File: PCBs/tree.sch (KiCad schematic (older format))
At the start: 31 parts, among them J1 Conn_01x06_Female, SW1 SW_Push_DPDT, SW2 SW_SPST, U1 Shift_Reg, U2 Shift_Reg, U3 Shift_Reg, U4 pic18f45k20

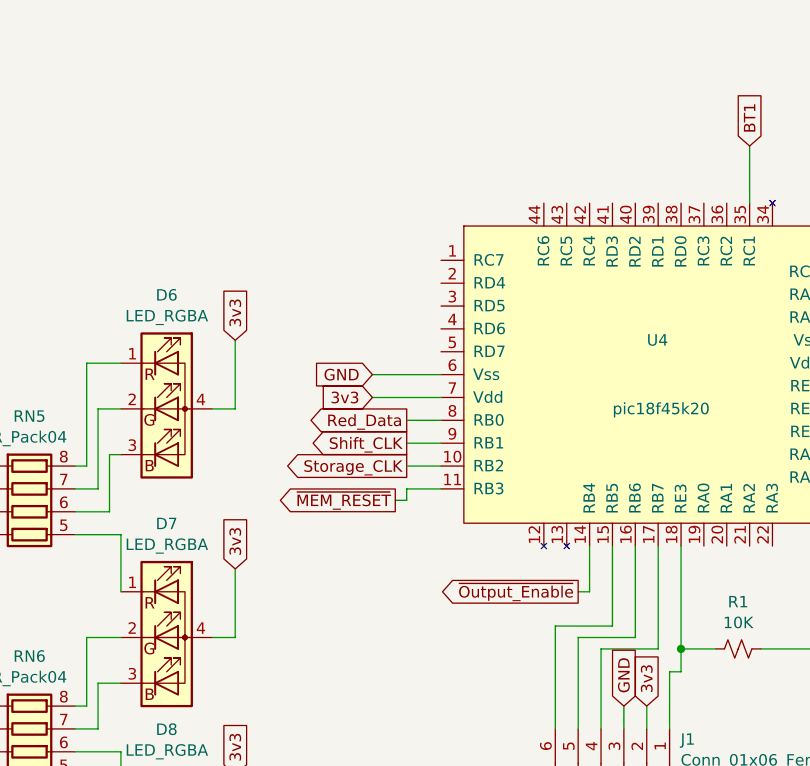
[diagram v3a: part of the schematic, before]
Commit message: Finished Bulk of routing. Reformated traces to use 6/6 mils as per board house rules.
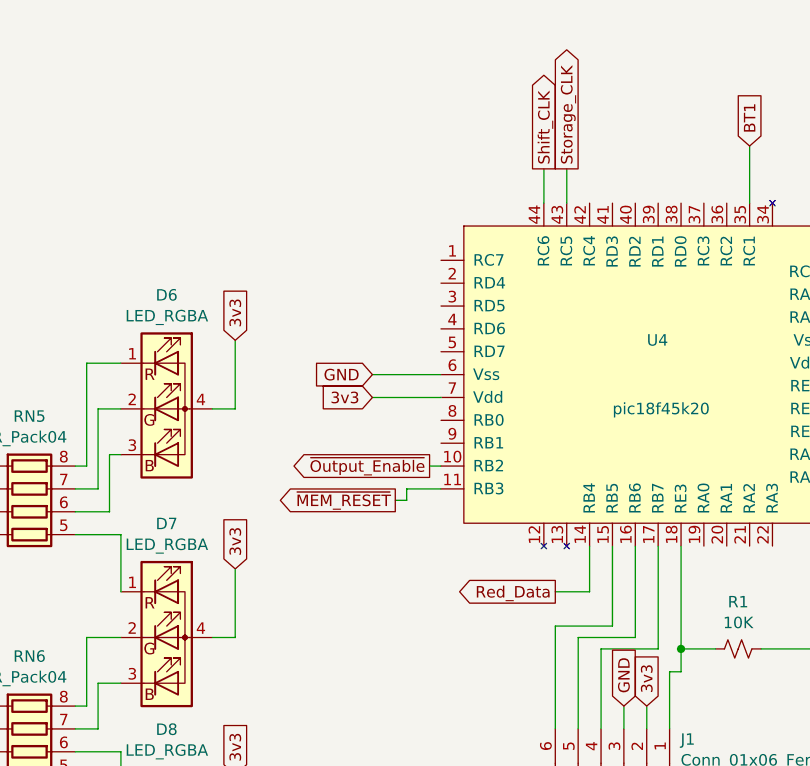
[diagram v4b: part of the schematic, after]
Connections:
- net Red_Data: now also U4.14 (RB4); no longer U4.8 (RB0)
- net Shift_CLK: now also U4.44 (RC6); no longer U4.9 (RB1)
- net Storage_CLK: now also U4.43 (RC5); no longer U4.10 (RB2)
- net ~Output_Enable~: now also U4.10 (RB2); no longer U4.14 (RB4)
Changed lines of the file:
@@
 Wire Wire Line
 	4200 3600 4050 3600
-Text GLabel 8400 2200 0    50   Output ~ 0
+Text GLabel 9050 2950 0    50   Output ~ 0
 Red_Data
 Wire Wire Line
-	8400 2200 8550 2200
+	9050 2950 9200 2950
 Text GLabel 4150 1750 2    50   Input ~ 0
 Shift_CLK
@@
 Wire Wire Line
 	4200 4250 4050 4250
-Text GLabel 8400 2300 0    50   Output ~ 0
+Text GLabel 9000 1100 1    50   Output ~ 0
 Shift_CLK
 Wire Wire Line
-	8400 2300 8550 2300
+	9000 1100 9000 1250
 Text GLabel 4150 2250 2    50   Input ~ 0
 Storage_CLK
@@
 Wire Wire Line
 	4200 4750 4050 4750
-Text GLabel 8400 2400 0    50   Output ~ 0
+Text GLabel 9100 1100 1    50   Output ~ 0
 Storage_CLK
 Wire Wire Line
-	8400 2400 8550 2400
+	9100 1100 9100 1250
 Text GLabel 2900 2300 0    50   Input ~ 0
 ~MEM_RESET~
@@
 Wire Wire Line
 	3000 4850 3150 4850
-Text GLabel 8350 2550 0    50   Output ~ 0
-~MEM_RESET~
-Text GLabel 9150 2950 0    50   Output ~ 0
+Text GLabel 8500 2400 0    50   Output ~ 0
 ~Output_Enable~
 Wire Wire Line
-	8350 2550 8400 2550
-Wire Wire Line
-	8400 2550 8400 2500
-Wire Wire Line
-	8400 2500 8550 2500
-Wire Wire Line
-	9150 2950 9200 2950
+	8500 2400 8550 2400
 Wire Wire Line
 	9200 2950 9200 2750
@@
 Wire Wire Line
 	2650 6750 2550 6750
+Wire Wire Line
+	8400 2500 8550 2500
+Wire Wire Line
+	8400 2550 8400 2500
+Wire Wire Line
+	8350 2550 8400 2550
+Text GLabel 8350 2550 0    50   Output ~ 0
+~MEM_RESET~
 $EndSCHEMATC

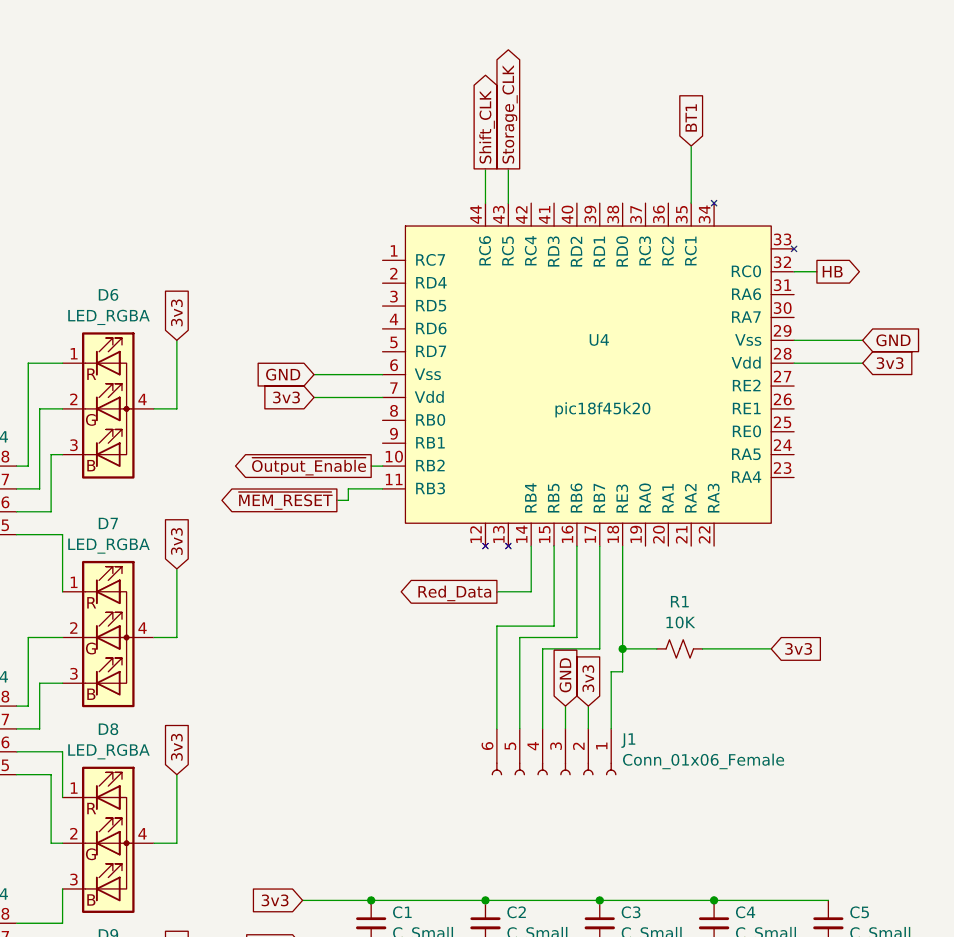
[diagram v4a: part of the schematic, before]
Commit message: Adding LPC804 as ARM processor for this branch
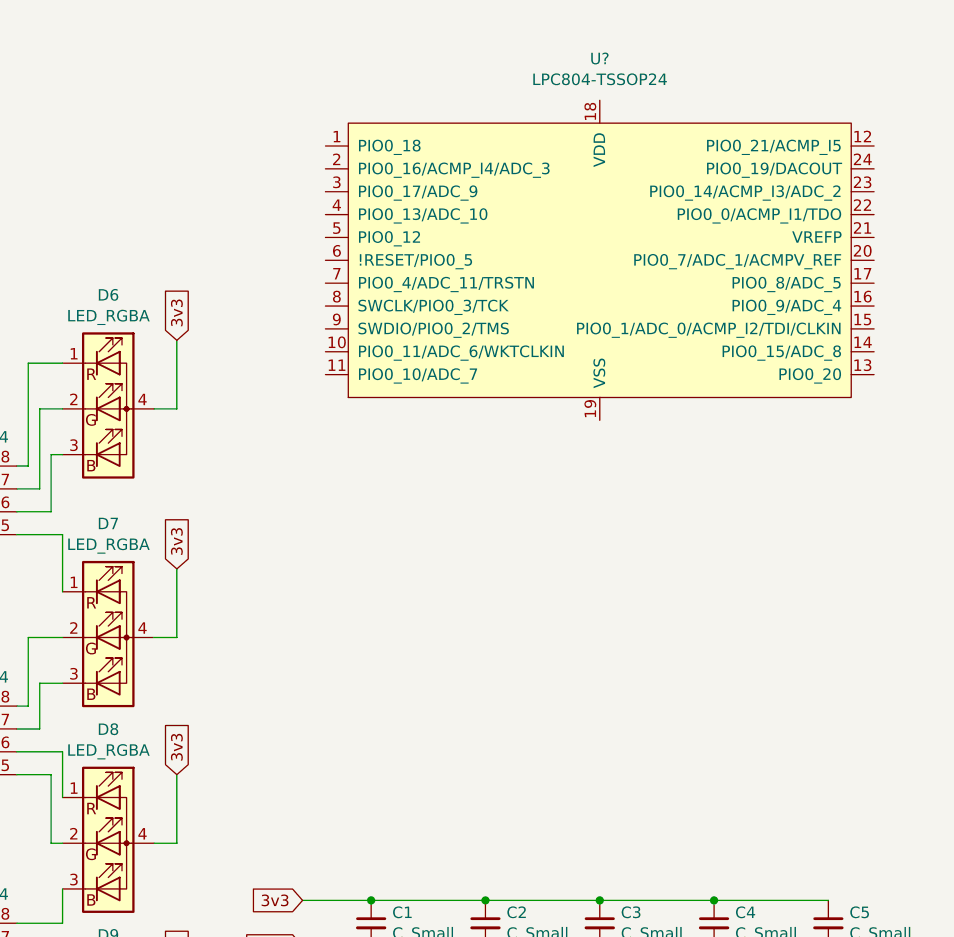
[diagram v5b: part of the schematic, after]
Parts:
- removed J1: Conn_01x06_Female, Connector_PinHeader_2.54mm:PinHeader_1x06_P2.54mm_Vertical, symbol Connector:Conn_01x06_Female
- removed R1: 10K, Resistor_SMD:R_0805_2012Metric, symbol Device:R_Small_US
- removed U4: pic18f45k20, Package_QFP:LQFP-44_10x10mm_P0.8mm, symbol pic18f45k20:pic18f45k20
- added U?: LPC804-TSSOP24, symbol MCU_NXP_LPC804:LPC804-TSSOP24
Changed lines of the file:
@@
 $EndDescr
-$Comp
-L pic18f45k20:pic18f45k20 U4
-U 1 1 6011DF0B
-P 9500 2000
-F 0 "U4" H 9450 2150 50  0000 L CNN
-F 1 "pic18f45k20" H 9300 1850 50  0000 L CNN
-F 2 "Package_QFP:LQFP-44_10x10mm_P0.8mm" H 9500 2000 50  0001 C CNN
-F 3 "" H 9500 2000 50  0001 C CNN
-	1    9500 2000
-	1    0    0    -1
-$EndComp
-$Comp
-L Connector:Conn_01x06_Female J1
-U 1 1 6011E5C4
-P 9350 3750
-F 0 "J1" V 9196 3998 50  0000 L CNN
-F 1 "Conn_01x06_Female" V 9287 3998 50  0000 L CNN
-F 2 "Connector_PinHeader_2.54mm:PinHeader_1x06_P2.54mm_Vertical" H 9350 3750 50  0001 C CNN
-F 3 "~" H 9350 3750 50  0001 C CNN
-	1    9350 3750
-	0    1    1    0
-$EndComp
-$Comp
-L Device:R_Small_US R1
-U 1 1 6011FC54
-P 9850 3200
-F 0 "R1" V 9645 3200 50  0000 C CNN
-F 1 "10K" V 9736 3200 50  0000 C CNN
-F 2 "Resistor_SMD:R_0805_2012Metric" H 9850 3200 50  0001 C CNN
-F 3 "~" H 9850 3200 50  0001 C CNN
-	1    9850 3200
-	0    1    1    0
-$EndComp
-Wire Wire Line
-	9050 3550 9050 3100
-Wire Wire Line
-	9050 3100 9300 3100
-Wire Wire Line
-	9300 3100 9300 2750
-Wire Wire Line
-	9150 3550 9150 3150
-Wire Wire Line
-	9150 3150 9400 3150
-Wire Wire Line
-	9400 3150 9400 2750
-Wire Wire Line
-	9250 3550 9250 3200
-Wire Wire Line
-	9250 3200 9500 3200
-Wire Wire Line
-	9500 3200 9500 2750
-Wire Wire Line
-	9600 2750 9600 3200
-Wire Wire Line
-	9600 3200 9750 3200
-Connection ~ 9600 3200
-Wire Wire Line
-	9600 3200 9600 3300
-Wire Wire Line
-	9600 3300 9550 3300
-Wire Wire Line
-	9550 3300 9550 3550
 $Comp
 L Device:LED_RGBA D7
@@
 Wire Wire Line
 	10000 4500 10500 4500
-Text GLabel 8250 2100 0    50   Input ~ 0
-3v3
-Wire Wire Line
-	8250 2100 8550 2100
-Text GLabel 10650 1950 2    50   Input ~ 0
-3v3
-Wire Wire Line
-	10650 1950 10350 1950
-Text GLabel 10250 3200 2    50   Input ~ 0
-3v3
-Wire Wire Line
-	10250 3200 9950 3200
-Text GLabel 8250 2000 0    50   Input ~ 0
-GND
-Wire Wire Line
-	8250 2000 8550 2000
-Text GLabel 10650 1850 2    50   Input ~ 0
-GND
-Wire Wire Line
-	10650 1850 10350 1850
 Text GLabel 4300 1650 2    50   Input ~ 0
 GND
@@
 Wire Wire Line
 	7650 4950 7550 4950
-Text GLabel 9450 3450 1    50   Input ~ 0
-3v3
-Wire Wire Line
-	9450 3450 9450 3550
-Text GLabel 9350 3450 1    50   Input ~ 0
-GND
-Wire Wire Line
-	9350 3450 9350 3550
 $Comp
 L Device:Battery_Cell BT1
@@
 Wire Wire Line
 	4200 3600 4050 3600
-Text GLabel 9050 2950 0    50   Output ~ 0
-Red_Data
-Wire Wire Line
-	9050 2950 9200 2950
 Text GLabel 4150 1750 2    50   Input ~ 0
 Shift_CLK
@@
 Wire Wire Line
 	4200 4250 4050 4250
-Text GLabel 9000 1100 1    50   Output ~ 0
-Shift_CLK
-Wire Wire Line
-	9000 1100 9000 1250
 Text GLabel 4150 2250 2    50   Input ~ 0
 Storage_CLK
@@
 Wire Wire Line
 	4200 4750 4050 4750
-Text GLabel 9100 1100 1    50   Output ~ 0
-Storage_CLK
-Wire Wire Line
-	9100 1100 9100 1250
 Text GLabel 2900 2300 0    50   Input ~ 0
 ~MEM_RESET~
@@
 Wire Wire Line
 	3000 4850 3150 4850
-Text GLabel 8500 2400 0    50   Output ~ 0
-~Output_Enable~
-Wire Wire Line
-	8500 2400 8550 2400
-Wire Wire Line
-	9200 2950 9200 2750
-Text GLabel 10450 1550 2    50   Output ~ 0
-HB
-Wire Wire Line
-	10450 1550 10350 1550
 $Comp
 L Device:R_Pack04 RN1
@@
 BT1
 Wire Wire Line
-	9900 1250 9900 1000
-Text GLabel 9900 1000 1    50   Input ~ 0
-BT1
-Wire Wire Line
 	3100 6750 3650 6750
 Wire Wire Line
@@
 Wire Wire Line
 	2650 6750 2550 6750
-Wire Wire Line
-	8400 2500 8550 2500
-Wire Wire Line
-	8400 2550 8400 2500
-Wire Wire Line
-	8350 2550 8400 2550
-Text GLabel 8350 2550 0    50   Output ~ 0
-~MEM_RESET~
+$Comp
+L MCU_NXP_LPC804:LPC804-TSSOP24 U?
+U 1 1 6024220D
+P 9500 1450
+F 0 "U?" H 9500 2281 50  0000 C CNN
+F 1 "LPC804-TSSOP24" H 9500 2190 50  0000 C CNN
+F 2 "" H 8800 1450 50  0001 C CNN
+F 3 "" H 8800 1450 50  0001 C CNN
+	1    9500 1450
+	1    0    0    -1
+$EndComp
 $EndSCHEMATC
